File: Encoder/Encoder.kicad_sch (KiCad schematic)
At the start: 60 parts, among them J1 Conn_01x02_Male, J2 Conn_01x04_Male, J3 Conn_01x04_Male, J4 Conn_01x04_Female, Q1 SSM3J332R, Q12 S8050, Q2 BSS138, Q3 SSM3J332R, SW1 SW_DIP_x05, SW2 SW_SPDT_White, SW3 SW_SPST, U1 AZ1084CD-3.3, U2 MAX3485, U3 AS5600, U4 STM32C011F6P6, Y1 48MHz

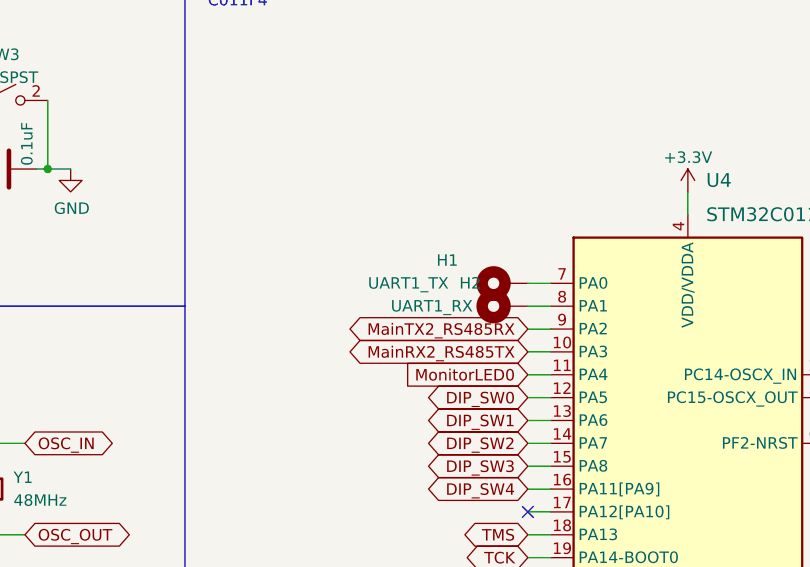
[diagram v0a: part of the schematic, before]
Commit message: 人力曲面配線中
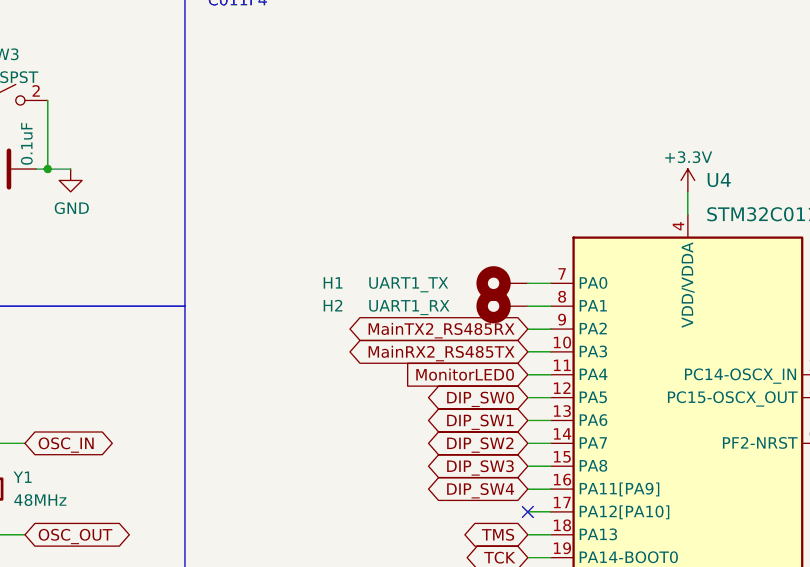
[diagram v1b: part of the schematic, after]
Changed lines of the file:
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@@
   (symbol (lib_id "Mechanical:MountingHole_Pad") (at 279.4 147.32 90) (unit 1)
     (in_bom yes) (on_board yes)
-    (property "Reference" "H2" (id 0) (at 274.32 144.78 90)
-      (effects (font (size 1.27 1.27)) (justify right))
-    )
-    (property "Value" "UART1_RX" (id 1) (at 266.7 147.32 90)
+    (property "Reference" "H2" (id 0) (at 259.08 147.32 90)
+      (effects (font (size 1.27 1.27)) (justify right))
+    )
+    (property "Value" "UART1_RX" (id 1) (at 264.16 147.32 90)
       (effects (font (size 1.27 1.27)) (justify right))
     )
@@
   (symbol (lib_id "Mechanical:MountingHole_Pad") (at 279.4 144.78 90) (unit 1)
     (in_bom yes) (on_board yes)
-    (property "Reference" "H1" (id 0) (at 271.78 142.24 90)
-      (effects (font (size 1.27 1.27)) (justify right))
-    )
+    (property "Reference" "H1" (id 0) (at 259.08 144.78 90)
+      (effects (font (size 1.27 1.27)) (justify right))
+    )
